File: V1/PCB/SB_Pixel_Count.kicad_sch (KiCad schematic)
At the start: 17 parts, among them J2 String1, J3 OLED, SW1 Test, U2 AMS1117-5.0, U4 74AHCT1G125, U4 INA219BxD, U5 RP2040-Tiny

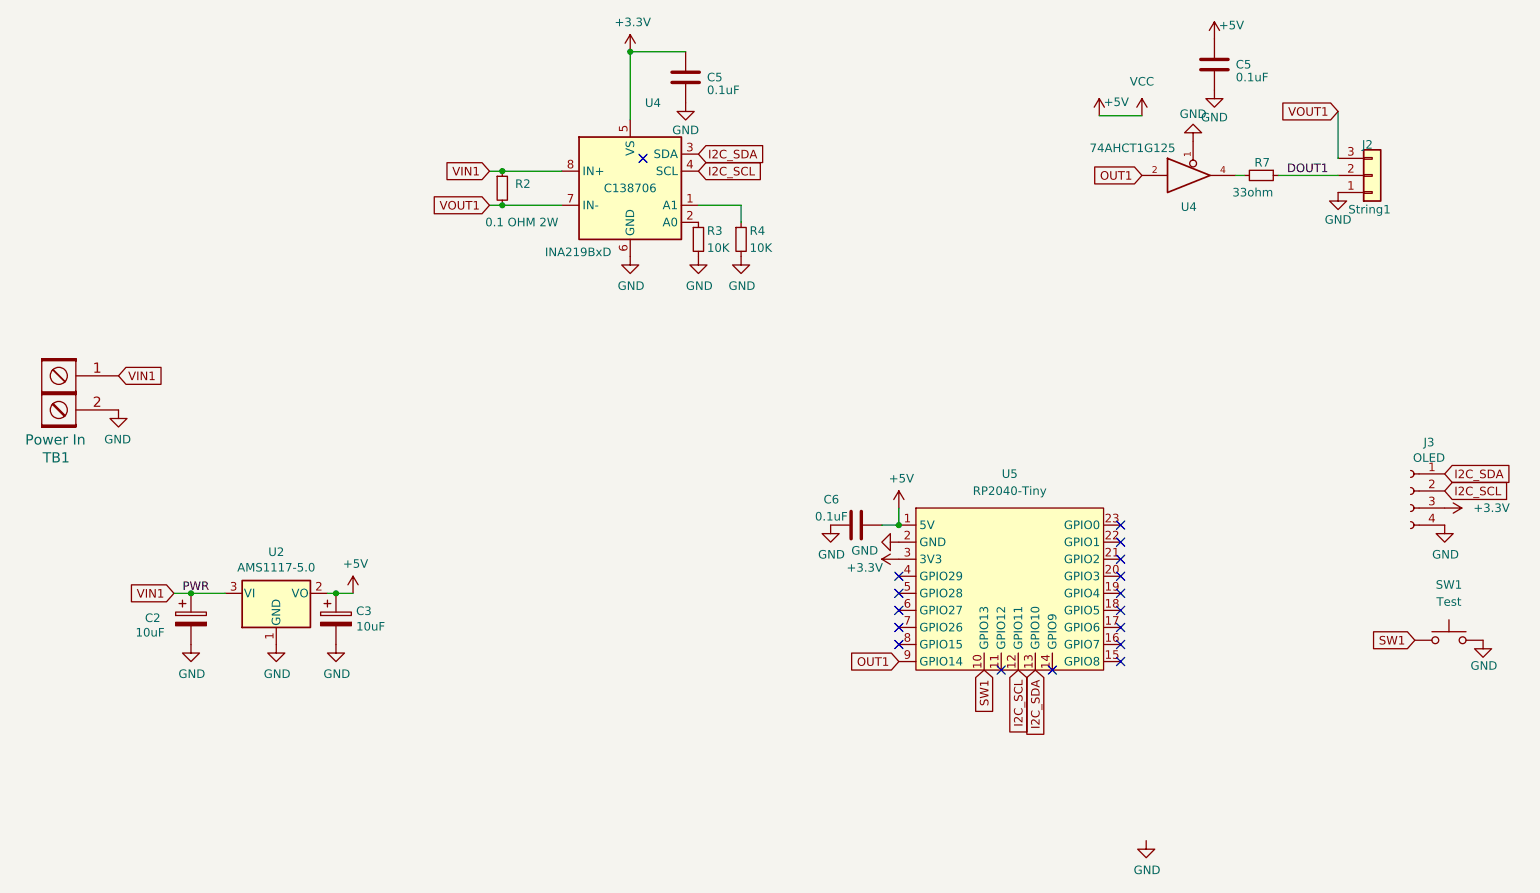
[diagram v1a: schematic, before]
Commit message: Add company name to title blocks; fix V3 Pro SW1/SW2 push-button DRC
Add (company "S&B Designs LLC") to V1/V2/V3 Pro's PCB and schematic
title blocks, matching V2 Lite, and add \${COMPANY} to each board's
silkscreen gr_text so it's printed on the physical board too.

Also includes KiCad-side board edits made while investigating the
SW1/SW2 "unconnected pad" DRC warnings on V3 Pro: added
lib/Scotts.pretty/SW_PUSH_6mm.kicad_mod, a copy of the standard
4-leg tactile switch footprint with unique pad numbers (1-4) instead
of the original's duplicated 1/1/2/2 numbering. The two redundant
mechanical-only legs (pads 3/4) are left with no net assigned, so
DRC's missing-connection check no longer applies to them. V3 Pro's
SW1/SW2 now use this footprint. Regenerated gerbers/BOM/fp-info-cache
reflect the resave.

Co-Authored-By: Claude Sonnet 5 <noreply@anthropic.com>
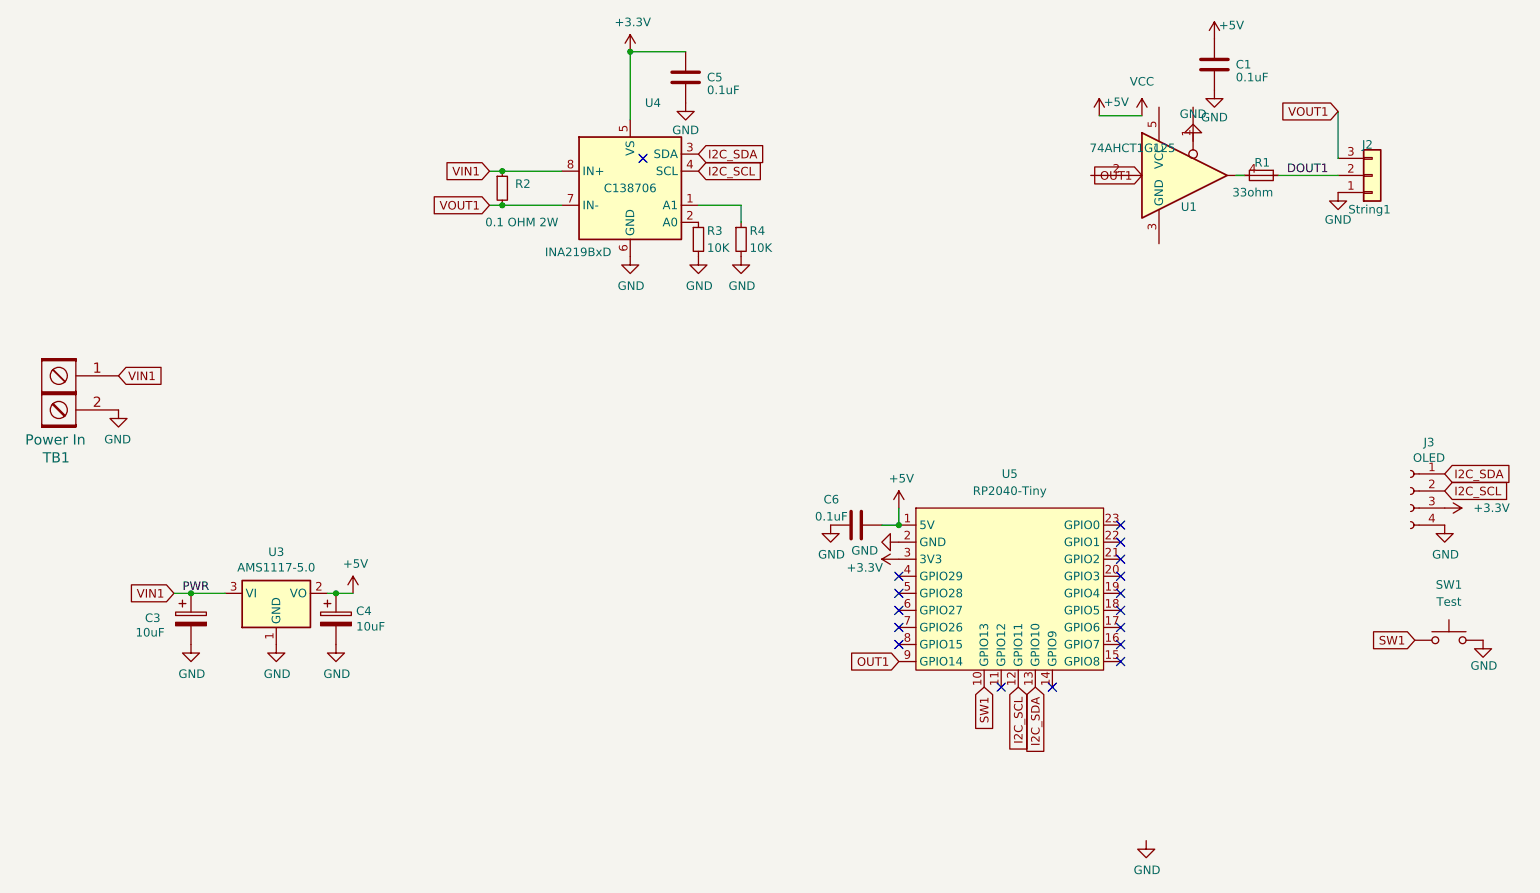
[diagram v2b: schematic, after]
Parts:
- renumbered C5 to C1, C2 to C3, C3 to C4, R7 to R1, U4 to U1, U2 to U3
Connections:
- net +5V: no longer U1.5 (VCC)
- net DOUT1: now also U1.4
- net GND: no longer U1.1, U1.3 (GND)
- net OUT1: no longer U1.2
- net at R1.2: no longer U1.4
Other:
- company: (none) -> S&B Designs LLC
- moved on the sheet: U5
